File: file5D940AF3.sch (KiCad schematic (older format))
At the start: 134 parts, among them CN1 KEYBOARD_20PIN_MALE, CN10 LED_CONNECTOR, CN2 USER_PORT_CON, CN3 CASSETTE_PORT_CON, CN4 SERIAL_BUS_CON, CN7 POWER_CON, CN8 CONTROL_PORT, CN9 CONTROL_PORT, Q1 2SC1815, Q2 2SC1815, Q3 TP298/2SD880, Q7 2SC1815, SW1 POWER_SWITCH, U1 CIA_U1, U2 CIA_U2, U20 556, U27 7408_U27, U28 4066_U28, U29 74LS74, U30 74LS193, U31 74LS629N, U32 MC4044, U7 6510_MPU, U8 7406N, Y1 Crystal

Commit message: Update V1.3
See readme
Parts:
- C36: value .1 -> 20pF
- C86: value ? -> 82pF
- R22: value NC -> 0R
- R52: value ? -> 330
- R53: value ? -> 100
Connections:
- net at C87.1, R23.2: now also R22.1
- no-connect marks 10 -> 9
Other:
- moved on the sheet: R22, R23, R53
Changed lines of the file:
@@
 Sheet 2 3
 Title "C64 Motherboard KU-14194HB"
-Date "2019-11-10"
-Rev "1.2"
+Date "2019-11-12"
+Rev "1.3"
 Comp "Commodore 1982"
 Comment1 "Retraced and schematics by bwack 2019"
@@
 AR Path="/5D940AF4/5D95B678" Ref="C36"  Part="1"
 F 0 "C36" H 10056 7482 50  0000 C CNN
-F 1 ".1" H 10045 7404 50  0000 C CNN
+F 1 "20pF" H 10100 7400 50  0000 C CNN
 F 2 "KU-14194HB-RevB-KiCad:RESISTOR" H 9900 7400 50  0001 C CNN
 F 3 "~" H 9900 7400 50  0001 C CNN
@@
 AR Path="/5DA2D2DF" Ref="C?"  Part="1"
 AR Path="/5D940AF4/5DA2D2DF" Ref="C86"  Part="1"
-F 0 "C86" V 9750 6400 50  0000 C CNN
-F 1 "?" V 9800 6400 50  0000 C CNN
+F 0 "C86" V 9700 6400 50  0000 C CNN
+F 1 "82pF" V 9776 6400 50  0000 C CNN
 F 2 "KU-14194HB-RevB-KiCad:RESISTOR" H 9900 6400 50  0001 C CNN
 F 3 "~" H 9900 6400 50  0001 C CNN
@@
 	0    1    1    0
 $EndComp
-Text Notes 10140 7512 2    50   ~ 0
-25V
 Wire Wire Line
 	10100 6400 10000 6400
@@
 U 1 1 5D88D3ED
 P 11350 4000
-F 0 "R27" H 11403 4038 39  0000 L CNN
-F 1 "500" H 11403 3963 39  0000 L CNN
+F 0 "R27" H 11403 4038 50  0000 L CNN
+F 1 "500" H 11403 3963 50  0000 L CNN
 F 2 "KU-14194HB-RevB-KiCad:POTMETER" H 11350 4000 39  0001 C CNN
 F 3 "" H 11350 4000 39  0001 C CNN
@@
 L KU-schematics-library:R_US_CUSTOM R?
 U 1 1 5D92D8A2
-P 11350 3650
+P 11350 3150
 AR Path="/5D92D8A2" Ref="R?"  Part="1"
 AR Path="/5D940AF4/5D92D8A2" Ref="R53"  Part="1"
-F 0 "R53" H 11400 3700 50  0000 L CNN
-F 1 "?" H 11405 3625 50  0000 L CNN
-F 2 "KU-14194HB-RevB-KiCad:RESISTOR" H 11350 3650 50  0001 C CNN
-F 3 "" H 11350 3650 50  0001 C CNN
-	1    11350 3650
+F 0 "R53" H 11150 3200 50  0000 L CNN
+F 1 "100" H 11150 3125 50  0000 L CNN
+F 2 "KU-14194HB-RevB-KiCad:RESISTOR" H 11350 3150 50  0001 C CNN
+F 3 "" H 11350 3150 50  0001 C CNN
+	1    11350 3150
 	1    0    0    -1
 $EndComp
@@
 AR Path="/5D940AF4/5D92E780" Ref="R52"  Part="1"
 F 0 "R52" H 11405 4282 50  0000 L CNN
-F 1 "?" H 11406 4209 50  0000 L CNN
+F 1 "330" H 11406 4209 50  0000 L CNN
 F 2 "KU-14194HB-RevB-KiCad:RESISTOR" H 11350 4250 50  0001 C CNN
 F 3 "" H 11350 4250 50  0001 C CNN
@@
 $EndComp
 Wire Wire Line
-	11350 3900 11350 3750
+	11350 3900 11350 3250
 $Comp
 L KU-14194HB-REV-B-KiCad-rescue:GND_SMALL-power-KU-14194HB-REV-B-KiCad-rescue U?
@@
 $EndComp
 Wire Wire Line
-	11350 3550 11350 2950
+	11350 3050 11350 2950
 Connection ~ 10800 2950
 Wire Wire Line
@@
 L KU-schematics-library:R_US_CUSTOM R?
 U 1 1 5E0D17B1
-P 12950 3150
+P 12950 3100
 AR Path="/5E0D17B1" Ref="R?"  Part="1"
 AR Path="/5D940AF4/5E0D17B1" Ref="R23"  Part="1"
-F 0 "R23" H 12750 3200 50  0000 L CNN
-F 1 "NC" H 12750 3125 50  0000 L CNN
-F 2 "KU-14194HB-RevB-KiCad:RESISTOR" H 12950 3150 50  0001 C CNN
-F 3 "" H 12950 3150 50  0001 C CNN
-	1    12950 3150
+F 0 "R23" H 12750 3150 50  0000 L CNN
+F 1 "NC" H 12750 3075 50  0000 L CNN
+F 2 "KU-14194HB-RevB-KiCad:RESISTOR" H 12950 3100 50  0001 C CNN
+F 3 "" H 12950 3100 50  0001 C CNN
+	1    12950 3100
 	1    0    0    -1
 $EndComp
 Wire Wire Line
-	12950 3050 12950 2950
+	12950 3000 12950 2950
 Wire Wire Line
 	12950 2950 12650 2950
@@
 L KU-14194HB-REV-B-KiCad-rescue:GND_SMALL-power-KU-14194HB-REV-B-KiCad-rescue #U?
 U 1 1 5E1390F2
-P 12950 3450
+P 12950 3500
 AR Path="/5E1390F2" Ref="#U?"  Part="1"
 AR Path="/5D940AF4/5E1390F2" Ref="#U0238"  Part="1"
-F 0 "#U0238" H 12950 3450 50  0001 C CNN
-F 1 "GND_SMALL" H 12950 3450 50  0001 C CNN
-F 2 "" H 12950 3450 50  0001 C CNN
-F 3 "" H 12950 3450 50  0001 C CNN
-	1    12950 3450
+F 0 "#U0238" H 12950 3500 50  0001 C CNN
+F 1 "GND_SMALL" H 12950 3500 50  0001 C CNN
+F 2 "" H 12950 3500 50  0001 C CNN
+F 3 "" H 12950 3500 50  0001 C CNN
+	1    12950 3500
 	1    0    0    -1
 $EndComp
@@
 L KU-schematics-library:R_US_CUSTOM R?
 U 1 1 5E13986B
-P 13300 3350
+P 13300 3400
 AR Path="/5E13986B" Ref="R?"  Part="1"
 AR Path="/5D940AF4/5E13986B" Ref="R22"  Part="1"
-F 0 "R22" H 13100 3400 50  0000 L CNN
-F 1 "NC" H 13100 3325 50  0000 L CNN
-F 2 "KU-14194HB-RevB-KiCad:RESISTOR" H 13300 3350 50  0001 C CNN
-F 3 "" H 13300 3350 50  0001 C CNN
-	1    13300 3350
+F 0 "R22" H 13100 3450 50  0000 L CNN
+F 1 "0R" H 13100 3375 50  0000 L CNN
+F 2 "KU-14194HB-RevB-KiCad:RESISTOR" H 13300 3400 50  0001 C CNN
+F 3 "" H 13300 3400 50  0001 C CNN
+	1    13300 3400
 	1    0    0    -1
 $EndComp
-NoConn ~ 13300 3250
 $Comp
 L KU-14194HB-REV-B-KiCad-rescue:GND_SMALL-power-KU-14194HB-REV-B-KiCad-rescue #U?
 U 1 1 5E19F876
-P 13300 3450
+P 13300 3500
 AR Path="/5E19F876" Ref="#U?"  Part="1"
 AR Path="/5D940AF4/5E19F876" Ref="#U0239"  Part="1"
-F 0 "#U0239" H 13300 3450 50  0001 C CNN
-F 1 "GND_SMALL" H 13300 3450 50  0001 C CNN
-F 2 "" H 13300 3450 50  0001 C CNN
-F 3 "" H 13300 3450 50  0001 C CNN
-	1    13300 3450
+F 0 "#U0239" H 13300 3500 50  0001 C CNN
+F 1 "GND_SMALL" H 13300 3500 50  0001 C CNN
+F 2 "" H 13300 3500 50  0001 C CNN
+F 3 "" H 13300 3500 50  0001 C CNN
+	1    13300 3500
 	1    0    0    -1
 $EndComp
@@
 Wire Wire Line
 	9000 2950 9150 2950
+Wire Wire Line
+	12950 3500 12950 3450
+Wire Wire Line
+	12950 3250 12950 3200
+Wire Wire Line
+	13300 3250 12950 3250
+Connection ~ 12950 3250
+Wire Wire Line
+	13300 3300 13300 3250
 Wire Bus Line
 	7750 7100 7750 7400

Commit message: V1.3 C70
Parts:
- C70: value ~ -> 15pF 5%
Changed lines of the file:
@@
 AR Path="/5D940AF4/5EFDA322" Ref="C70"  Part="1"
 F 0 "C70" H 10100 3550 50  0000 C CNN
-F 1 "~" H 10142 3617 50  0000 C CNN
+F 1 "15pF 5%" H 10016 3477 50  0000 C CNN
 F 2 "KU-14194HB-RevB-KiCad:RESISTOR" H 10250 3550 50  0001 C CNN
 F 3 "~" H 10250 3550 50  0001 C CNN

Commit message: value updates
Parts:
- C88: value 1000uF -> 470uF
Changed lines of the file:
@@
 P 9850 8100
 F 0 "C88" H 9957 8096 50  0000 L CNN
-F 1 "1000uF" H 9906 8022 50  0000 L CNN
+F 1 "470uF" H 9906 8022 50  0000 L CNN
 F 2 "KU-14194HB-RevB-KiCad:LARGE_ELECTROLYTIC_33x18_P38.10mm_AXIAL_TH" H 9850 8100 50  0001 C CNN
 F 3 "~" H 9850 8100 50  0001 C CNN
@@
 	9850 7950 9700 7950
 Text Notes 10111 8289 2    50   ~ 0
-25V
+50V
 Wire Wire Line
 	9850 8000 9850 7950

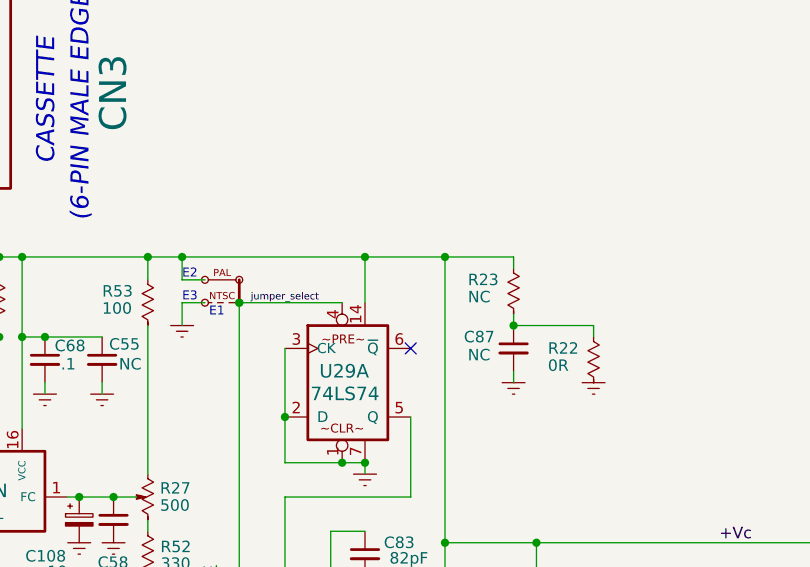
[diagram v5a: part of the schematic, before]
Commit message: moved silkscreen from board to footprint library
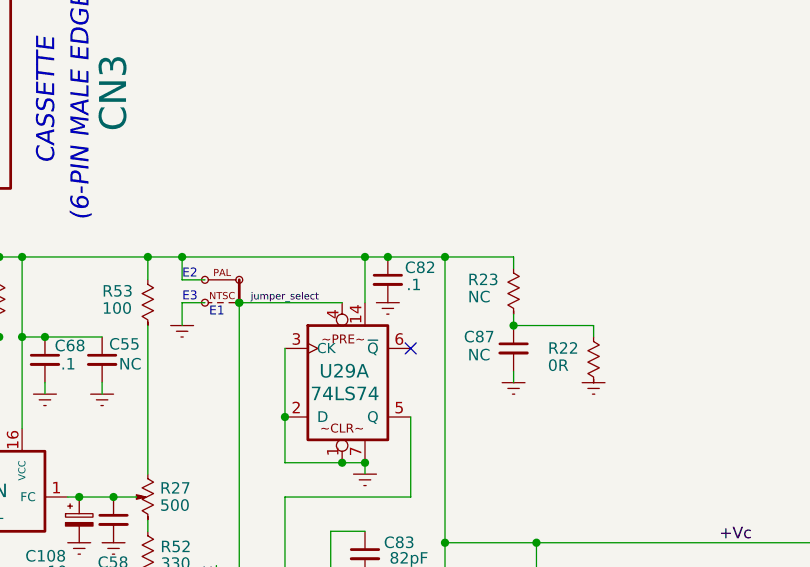
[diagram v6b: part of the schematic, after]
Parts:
- added C82: .1, KU-14194HB-RevB-KiCad:CAP_P5.08mm, symbol Device:C_Small
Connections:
- net +Vc: now also C82.1
- net Earth: now also C82.2
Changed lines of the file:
@@
 EESchema Schematic File Version 4
-LIBS:KU-14194HB-REV-B-KiCad-cache
 EELAYER 30 0
 EELAYER END
@@
 	12650 2950 12650 4200
 Wire Wire Line
-	12300 2950 12650 2950
+	12300 2950 12400 2950
 Connection ~ 12650 4200
 Wire Wire Line
@@
 Wire Bus Line
 	7050 3550 7050 8400
+$Comp
+L Device:C_Small C?
+U 1 1 6019A4BB
+P 12400 3050
+AR Path="/6019A4BB" Ref="C?"  Part="1"
+AR Path="/5D940AF4/6019A4BB" Ref="C82"  Part="1"
+F 0 "C82" H 12542 3103 50  0000 C CNN
+F 1 ".1" H 12514 3028 50  0000 C CNN
+F 2 "KU-14194HB-RevB-KiCad:CAP_P5.08mm" H 12400 3050 50  0001 C CNN
+F 3 "~" H 12400 3050 50  0001 C CNN
+	1    12400 3050
+	1    0    0    -1
+$EndComp
+Connection ~ 12400 2950
+Wire Wire Line
+	12400 2950 12650 2950
+$Comp
+L KU-14194HB-REV-B-KiCad-rescue:GND_SMALL-power-KU-14194HB-REV-B-KiCad-rescue-KU-14194HB-REV-B-KiCad-rescue #U?
+U 1 1 601A23C4
+P 12400 3150
+AR Path="/601A23C4" Ref="#U?"  Part="1"
+AR Path="/5D940AF4/601A23C4" Ref="#U?"  Part="1"
+F 0 "#U?" H 12400 3150 50  0001 C CNN
+F 1 "GND_SMALL" H 12400 3150 50  0001 C CNN
+F 2 "" H 12400 3150 50  0001 C CNN
+F 3 "" H 12400 3150 50  0001 C CNN
+	1    12400 3150
+	1    0    0    -1
+$EndComp
 $EndSCHEMATC
